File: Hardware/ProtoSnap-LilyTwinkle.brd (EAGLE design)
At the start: 72.4 x 58.4 mm, 41 parts, among them U1 ATTINY85

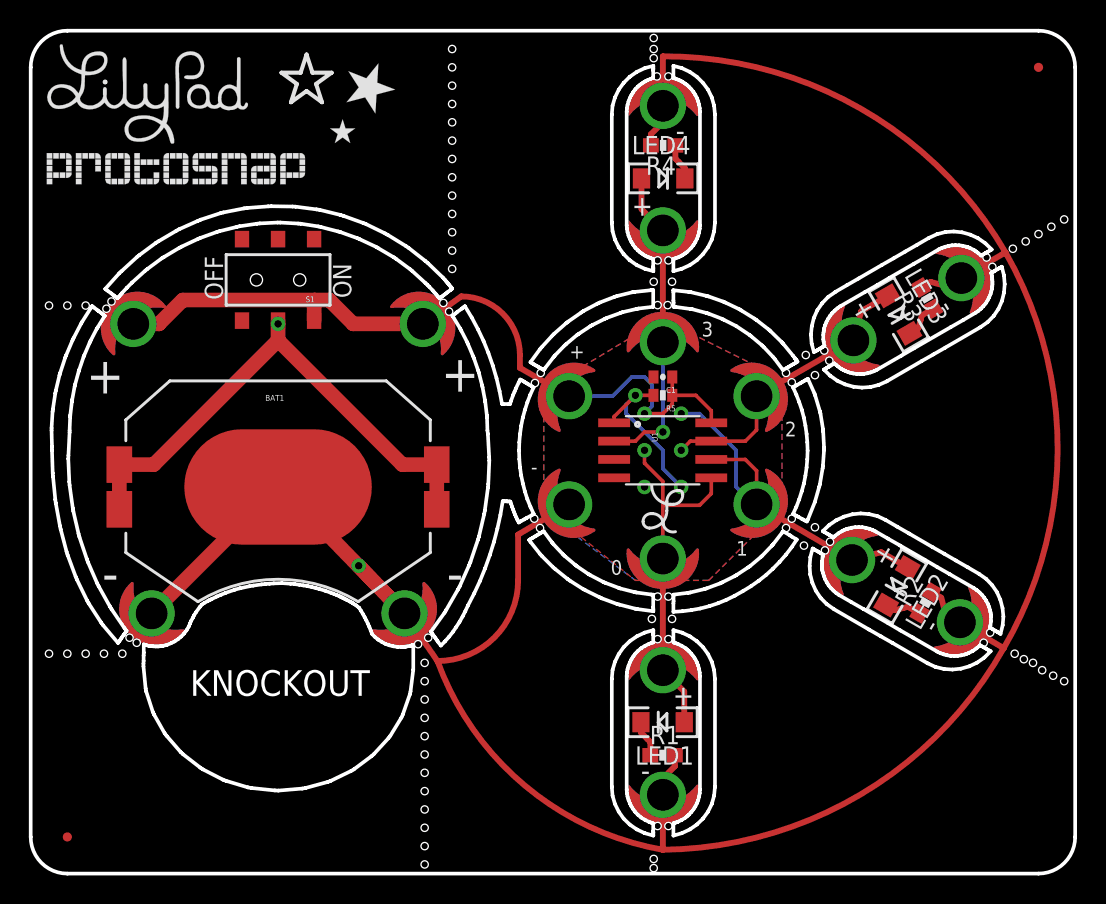
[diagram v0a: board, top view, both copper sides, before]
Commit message: V10 commit; files as proposed for production. Changes: - BMASK added to programming vias - Pin numbers moved onto masked area on top side - Pin numbers added to bottom - Pin 1 marker added to programming header - Position of snapping holes tweaked slightly for durability improvement
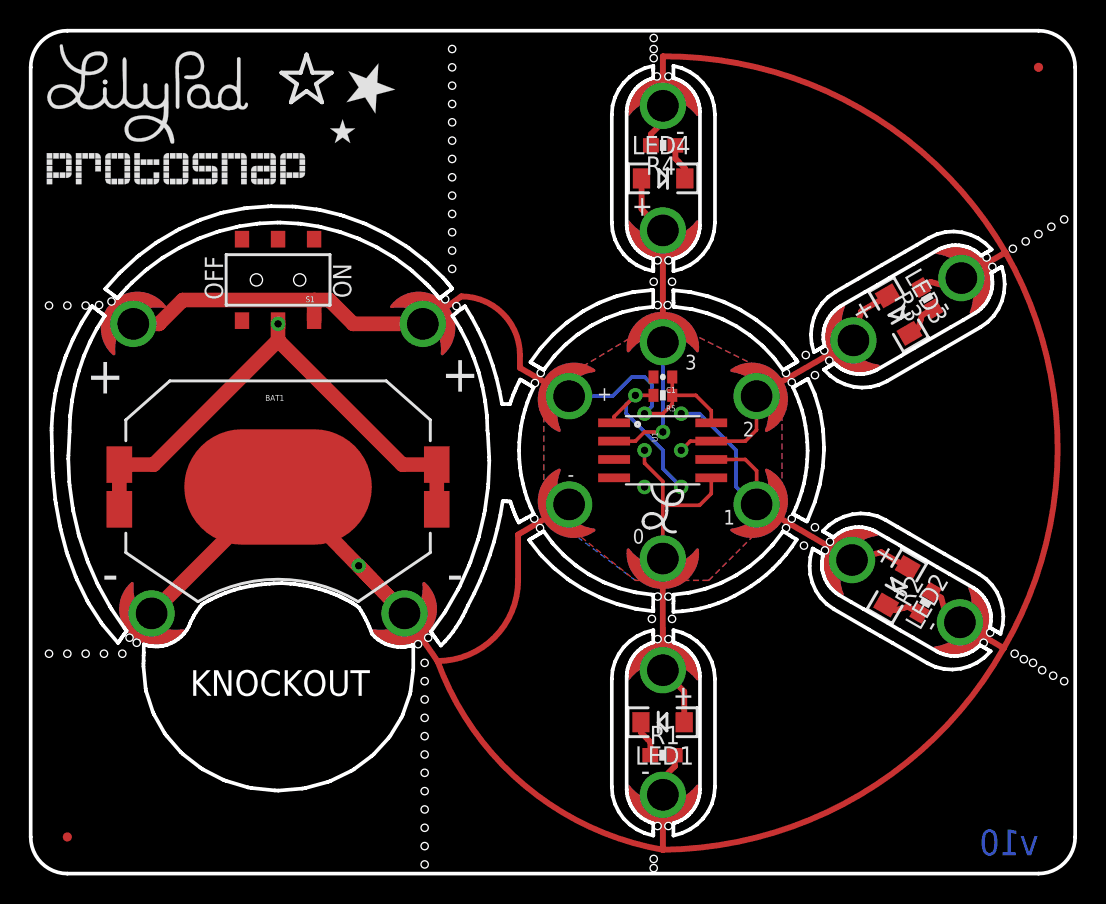
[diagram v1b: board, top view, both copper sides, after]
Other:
- board text added: "v10"
